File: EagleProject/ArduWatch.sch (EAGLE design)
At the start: 31 parts, among them IC1 DS1307Z, IC2 MCP73831, J1 FTS-105-01-L-D, Q1 32.768Hz, U2 ATMEGA328P-AU

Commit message: Starting Schematic
Starting Schematic in Eagle
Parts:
- LED1: value (none) -> Red
- LED2: value (none) -> Green
- renumbered PAD1 to USB+, PAD2 to USB-, PAD3 to BATTERY+, PAD4 to BATTERY-
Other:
- note added: "Battery 3,7V 140mAh"
- note added: "USB battery charger"
- note removed: "Bateria 3,7V"
- note removed: "Ładowarka USB"
- moved on the sheet: H1, H2, H3, H4, H5, J1, R7, U2

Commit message: Schematic V0.2.0
Schematic version 0.2.0
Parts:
- removed BATTERY+, BATTERY-: WIREPAD2,54/0,8, wirepad:WIREPAD2,54/0,8
- removed C4: 100nF, Kemet_By_element14_Batch_1:C1206C104K1RACTU
- removed H1, H2, H3, H4: MOUNT-HOLE3.0, holes:MOUNT-HOLE3.0
- removed LED2: Green, adafruit:LEDCHIPLED_1206
- removed R5: 10K Ohms, Multicomp_By_element14_Batch_1:MC0.125W12061%10K
- removed R6: 4.7 KOhm, Panasonic_By_element14_Batch_1:ERJ-8ENF4701V
- removed U$1: BATERY3,7V, Podreczne:BATERY3,7V
- removed U2: ATMEGA328P-AU, Atmel_By_element14_Batch_1-00:ATMEGA328P-AU
- added B+, B-: WIREPAD2,54/0,8, wirepad:WIREPAD2,54/0,8
- added C5: 0.1µF, AVX_By_element14_Batch_1:1206YC104KAT2A
- added U1: ATMEGA328P_TQFP, SparkFun-DigitalIC:ATMEGA328P_TQFP
- S1: value (none) -> Button1
- S2: value (none) -> Button2
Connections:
- removed net N$7: LED2.A, R6.R2
- removed net SQW: IC1.SQW, LED2.C, R5.R2
- new net D10: 1,3"OLED1.CS, U1.PB2(SS/OC1B)
- new net D8: 1,3"OLED1.RST, U1.PB0(ICP)
- new net D9: 1,3"OLED1.DC, U1.PB1(OC1A)
- net BUTTON1: now also U1.PD2(INT0)
- net BUTTON2: now also U1.PD3(INT1)
- net D11: now also 1,3"OLED1.D1, U1.PB3(MOSI/OC2)
- net D12: now also U1.PB4(MISO)
- net D13: now also 1,3"OLED1.D0, U1.PB5(SCK)
- net GND: now also 1,3"OLED1.GND, B-.P, C5.C1, U1.AGND, U1.GND@3, U1.GND@5; no longer BATTERY-.P, C4.C1, R6.R1, U$1.-
- net N$2: now also Q1.2; no longer Q1.1
- net N$5: now also Q1.1; no longer Q1.2
- net RESET: now also U1.PC6(/RESET); no longer U2.PC6
- net SCL: now also U1.PC5(ADC5/SCL)
- net SDA: now also U1.PC4(ADC4/SDA)
- net VCC: now also 1,3"OLED1.VCC, B+.P, C5.C2, U1.AVCC, U1.PC0(ADC0), U1.VCC@4, U1.VCC@6; no longer BATTERY+.P, C4.C2, R5.R1, U$1.+
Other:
- note added: "Buttons"
- note added: "Power"
- note removed: "Battery 3,7V 140mAh"
- note removed: "Przyciski"
- note removed: "Ładowanie baterii"
- moved on the sheet: C1, C2, C3, H5, IC2, LED1, Q1, R1, R2, R7, USB+, USB-

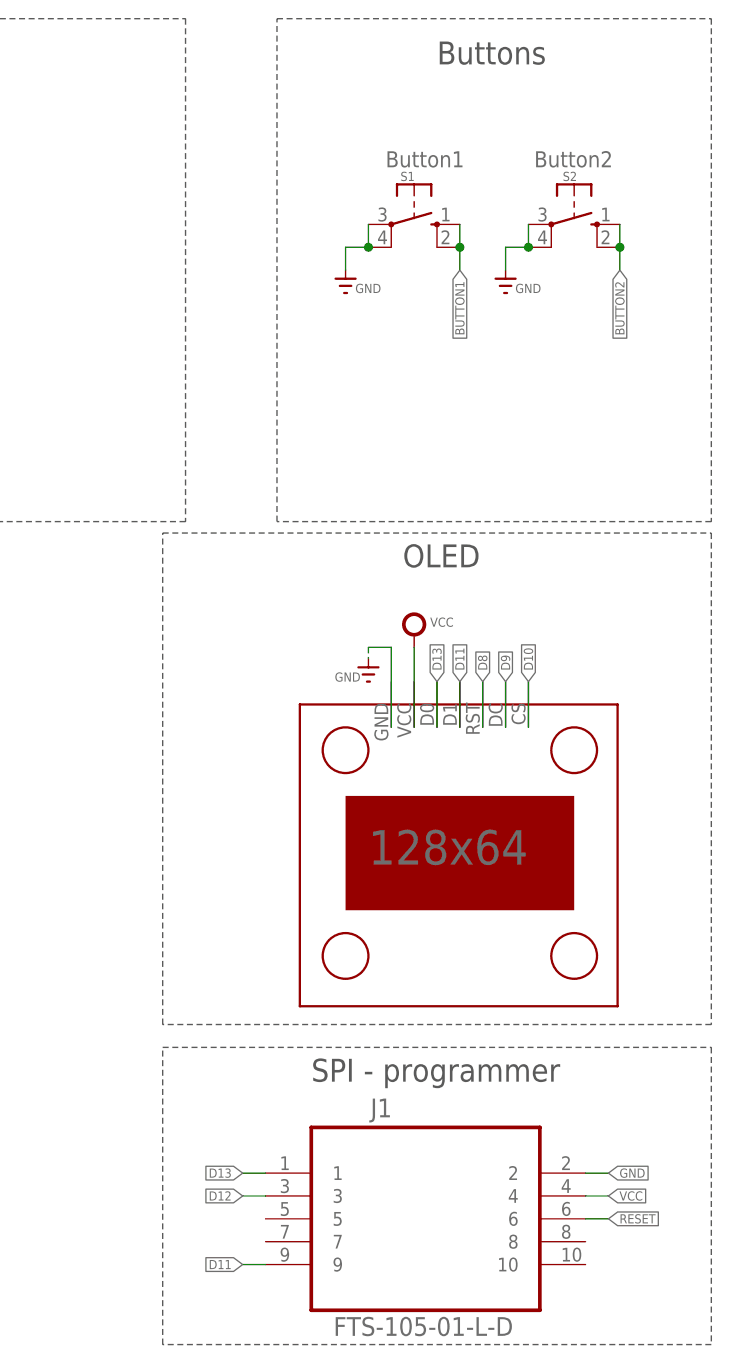
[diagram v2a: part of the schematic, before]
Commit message: Board V0.1.0
Update board to version 0.1.0
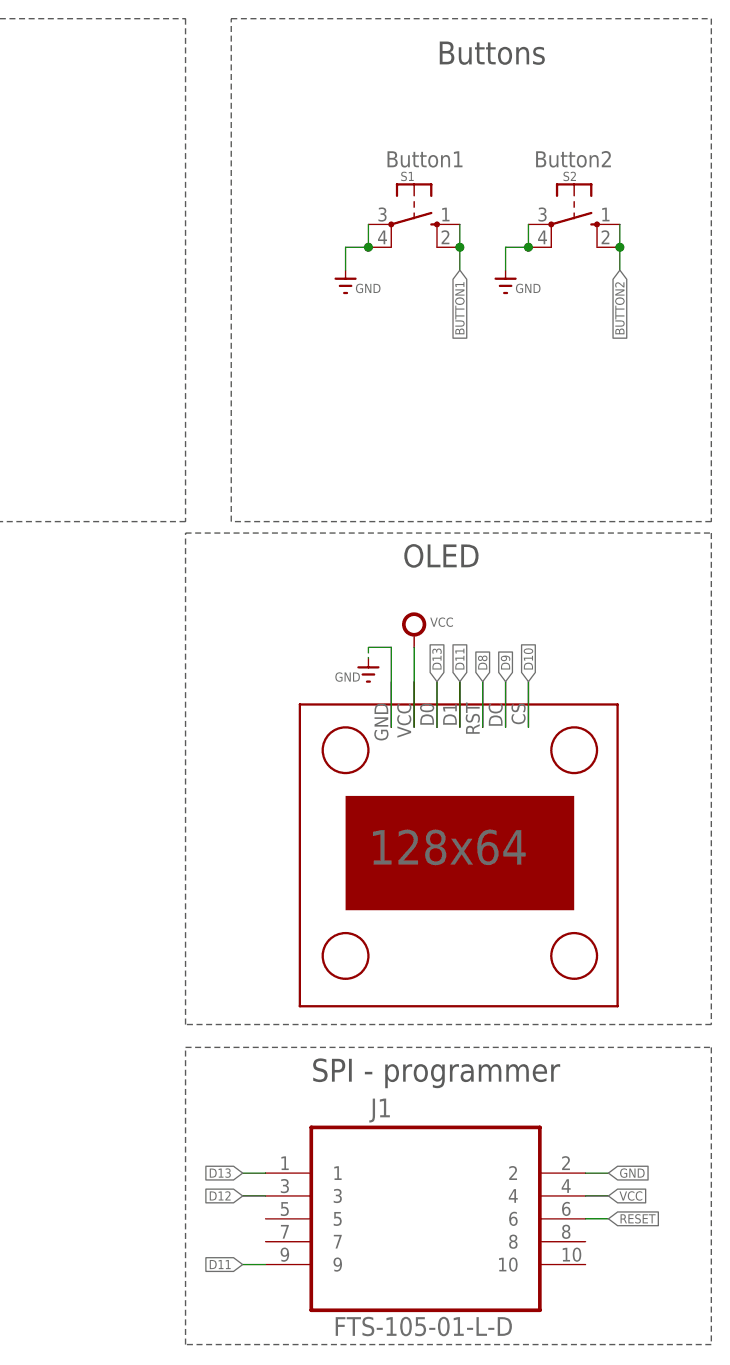
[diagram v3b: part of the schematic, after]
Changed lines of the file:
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@@
 <wire x1="101.6" y1="119.38" x2="101.6" y2="175.26" width="0.1524" layer="97" style="longdash"/>
 <text x="142.24" y="170.18" size="2.54" layer="97">RTC</text>
-<wire x1="200.66" y1="175.26" x2="248.92" y2="175.26" width="0.1524" layer="97" style="longdash"/>
+<wire x1="195.58" y1="175.26" x2="248.92" y2="175.26" width="0.1524" layer="97" style="longdash"/>
 <wire x1="248.92" y1="175.26" x2="248.92" y2="119.38" width="0.1524" layer="97" style="longdash"/>
-<wire x1="248.92" y1="119.38" x2="200.66" y2="119.38" width="0.1524" layer="97" style="longdash"/>
-<wire x1="200.66" y1="119.38" x2="200.66" y2="175.26" width="0.1524" layer="97" style="longdash"/>
+<wire x1="248.92" y1="119.38" x2="195.58" y2="119.38" width="0.1524" layer="97" style="longdash"/>
+<wire x1="195.58" y1="119.38" x2="195.58" y2="175.26" width="0.1524" layer="97" style="longdash"/>
 <text x="218.44" y="170.18" size="2.54" layer="97">Buttons</text>
-<wire x1="187.96" y1="118.11" x2="248.92" y2="118.11" width="0.1524" layer="97" style="longdash"/>
+<wire x1="190.5" y1="118.11" x2="248.92" y2="118.11" width="0.1524" layer="97" style="longdash"/>
 <wire x1="248.92" y1="118.11" x2="248.92" y2="63.5" width="0.1524" layer="97" style="longdash"/>
-<wire x1="248.92" y1="63.5" x2="187.96" y2="63.5" width="0.1524" layer="97" style="longdash"/>
-<wire x1="187.96" y1="63.5" x2="187.96" y2="118.11" width="0.1524" layer="97" style="longdash"/>
+<wire x1="248.92" y1="63.5" x2="190.5" y2="63.5" width="0.1524" layer="97" style="longdash"/>
+<wire x1="190.5" y1="63.5" x2="190.5" y2="118.11" width="0.1524" layer="97" style="longdash"/>
 <text x="214.63" y="114.3" size="2.54" layer="97">OLED</text>
-<wire x1="187.96" y1="60.96" x2="248.92" y2="60.96" width="0.1524" layer="97" style="longdash"/>
+<wire x1="190.5" y1="60.96" x2="248.92" y2="60.96" width="0.1524" layer="97" style="longdash"/>
 <wire x1="248.92" y1="60.96" x2="248.92" y2="27.94" width="0.1524" layer="97" style="longdash"/>
-<wire x1="248.92" y1="27.94" x2="187.96" y2="27.94" width="0.1524" layer="97" style="longdash"/>
-<wire x1="187.96" y1="27.94" x2="187.96" y2="60.96" width="0.1524" layer="97" style="longdash"/>
+<wire x1="248.92" y1="27.94" x2="190.5" y2="27.94" width="0.1524" layer="97" style="longdash"/>
+<wire x1="190.5" y1="27.94" x2="190.5" y2="60.96" width="0.1524" layer="97" style="longdash"/>
 <text x="204.47" y="57.15" size="2.54" layer="97">SPI - programmer</text>
 </plain>

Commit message: PCB release
PCB release
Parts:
- H5: value MOUNT-HOLE4.1 -> MOUNT-HOLE3.0; device holes:MOUNT-HOLE4.1 -> holes:MOUNT-HOLE3.0
- USB+, USB-: value WIREPAD2,54/0,8 -> WIREPAD3,81/1,1; device wirepad:WIREPAD2,54/0,8 -> wirepad:WIREPAD3,81/1,1
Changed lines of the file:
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@@
 <part name="Q1" library="crystal" deviceset="CRYSTAL" device="TC26H" value="32.768Hz"/>
 <part name="IC2" library="microchip-update" deviceset="MCP73831" device=""/>
-<part name="USB+" library="wirepad" deviceset="WIREPAD" device="2,54/0,8"/>
-<part name="USB-" library="wirepad" deviceset="WIREPAD" device="2,54/0,8"/>
+<part name="USB+" library="wirepad" deviceset="WIREPAD" device="3,81/1,1" value="WIREPAD3,81/1,1"/>
+<part name="USB-" library="wirepad" deviceset="WIREPAD" device="3,81/1,1" value="WIREPAD3,81/1,1"/>
 <part name="GND1" library="supply" deviceset="GND" device=""/>
 <part name="V1" library="supply" deviceset="VUSB" device=""/>
@@
 <part name="V7" library="supply" deviceset="VCC" device=""/>
 <part name="R7" library="Multicomp_By_element14_Batch_1" deviceset="MC0.125W12061%10K" device="" value="10K Ohms"/>
-<part name="H5" library="holes" deviceset="MOUNT-HOLE" device="4.1"/>
+<part name="H5" library="holes" deviceset="MOUNT-HOLE" device="3.0" value="MOUNT-HOLE3.0"/>
 <part name="J1" library="SAMTEC-HTSW-FTxx_By_element14_Batch_1" deviceset="FTS-105-01-L-D" device=""/>
 <part name="FRAME1" library="frames" deviceset="A4L-LOC" device="" value="Frame"/>
@@
 <sheet>
 <plain>
-<text x="17.78" y="160.02" size="1.778" layer="97">USB battery charger</text>
+<text x="12.7" y="154.94" size="1.778" layer="97">USB battery charger</text>
 <wire x1="5.08" y1="175.26" x2="99.06" y2="175.26" width="0.1524" layer="97" style="longdash"/>
 <wire x1="99.06" y1="175.26" x2="99.06" y2="119.38" width="0.1524" layer="97" style="longdash"/>

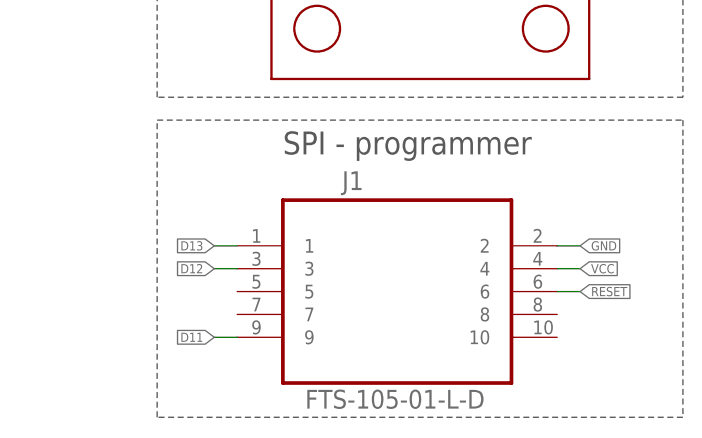
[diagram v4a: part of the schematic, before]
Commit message: PCB - SPI as Arduino
Change connector for SPI Target
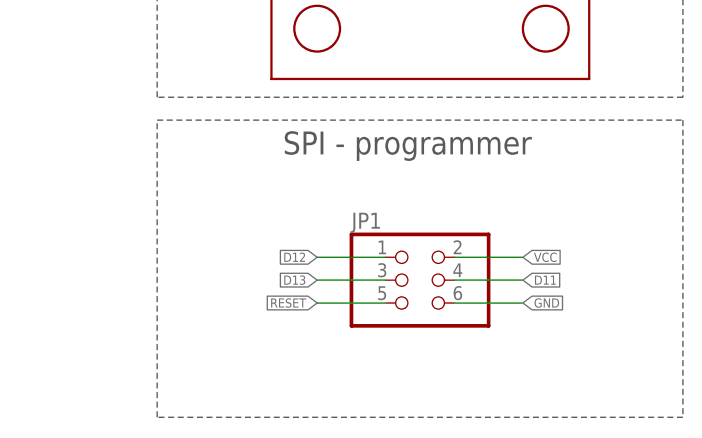
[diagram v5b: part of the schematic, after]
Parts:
- removed J1: FTS-105-01-L-D, SAMTEC-HTSW-FTxx_By_element14_Batch_1:FTS-105-01-L-D
- added JP1: (no value), pinhead:PINHD-2X3
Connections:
- net D11: now also JP1.4; no longer J1.9
- net D12: now also JP1.1; no longer J1.3
- net D13: now also JP1.3; no longer J1.1
- net GND: now also JP1.6; no longer J1.2
- net RESET: now also JP1.5; no longer J1.6
- net VCC: now also JP1.2; no longer J1.4
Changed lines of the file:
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@@
 <part name="R7" library="Multicomp_By_element14_Batch_1" deviceset="MC0.125W12061%10K" device="" value="10K Ohms"/>
 <part name="H5" library="holes" deviceset="MOUNT-HOLE" device="3.0" value="MOUNT-HOLE3.0"/>
-<part name="J1" library="SAMTEC-HTSW-FTxx_By_element14_Batch_1" deviceset="FTS-105-01-L-D" device=""/>
 <part name="FRAME1" library="frames" deviceset="A4L-LOC" device="" value="Frame"/>
 <part name="V6" library="supply" deviceset="VCC" device=""/>
@@
 <part name="GND11" library="supply" deviceset="GND" device=""/>
 <part name="V8" library="supply" deviceset="VCC" device=""/>
+<part name="JP1" library="pinhead" deviceset="PINHD-2X3" device=""/>
 </parts>
 <sheets>
@@
 <attribute name="VALUE" x="61.468" y="129.4638" size="1.016" layer="96" rot="R180"/>
 </instance>
-<instance part="J1" gate="A" x="217.17" y="44.45" smashed="yes">
-<attribute name="NAME" x="211.0486" y="53.1876" size="2.0828" layer="95" ratio="10" rot="SR0"/>
-<attribute name="VALUE" x="206.9338" y="28.9052" size="2.0828" layer="96" ratio="10" rot="SR0"/>
-</instance>
 <instance part="FRAME1" gate="G$1" x="0" y="0"/>
 <instance part="V6" gate="VCC" x="57.15" y="92.71" smashed="yes">
@@
 <attribute name="VALUE" x="126.238" y="92.456" size="1.016" layer="96"/>
 </instance>
+<instance part="JP1" gate="A" x="218.44" y="43.18"/>
 </instances>
 <busses>
@@
 </segment>
 <segment>
-<pinref part="J1" gate="A" pin="2"/>
-<wire x1="234.95" y1="46.99" x2="237.49" y2="46.99" width="0.1524" layer="91"/>
-<label x="237.49" y="46.99" size="1.016" layer="95" xref="yes"/>
-</segment>
-<segment>
 <pinref part="GND10" gate="1" pin="GND"/>
 <pinref part="C5" gate="A" pin="C1"/>
@@
 <junction x="68.58" y="39.37"/>
 </segment>
+<segment>
+<pinref part="JP1" gate="A" pin="6"/>
+<wire x1="223.52" y1="40.64" x2="231.14" y2="40.64" width="0.1524" layer="91"/>
+<label x="231.14" y="40.64" size="1.016" layer="95" xref="yes"/>
+</segment>
 </net>
 <net name="N$4" class="0">
@@
 <wire x1="71.12" y1="107.95" x2="71.12" y2="106.68" width="0.1524" layer="91"/>
 <pinref part="R7" gate="A" pin="R1"/>
-</segment>
-<segment>
-<pinref part="J1" gate="A" pin="4"/>
-<wire x1="234.95" y1="44.45" x2="237.49" y2="44.45" width="0.1524" layer="91"/>
-<label x="237.49" y="44.45" size="1.016" layer="95" xref="yes"/>
 </segment>
 <segment>
@@
 <pinref part="V8" gate="VCC" pin="VCC"/>
 </segment>
+<segment>
+<pinref part="JP1" gate="A" pin="2"/>
+<wire x1="223.52" y1="45.72" x2="231.14" y2="45.72" width="0.1524" layer="91"/>
+<label x="231.14" y="45.72" size="1.016" layer="95" xref="yes"/>
+</segment>
 </net>
 <net name="SCL" class="0">
@@
 </segment>
 <segment>
-<pinref part="J1" gate="A" pin="1"/>
-<wire x1="199.39" y1="46.99" x2="196.85" y2="46.99" width="0.1524" layer="91"/>
-<label x="196.85" y="46.99" size="1.016" layer="95" rot="R180" xref="yes"/>
-</segment>
-<segment>
 <pinref part="U1" gate="U$1" pin="PB5(SCK)"/>
 <wire x1="121.92" y1="34.29" x2="125.73" y2="34.29" width="0.1524" layer="91"/>
 <label x="125.73" y="34.29" size="1.016" layer="95" xref="yes"/>
 </segment>
+<segment>
+<pinref part="JP1" gate="A" pin="3"/>
+<wire x1="215.9" y1="43.18" x2="208.28" y2="43.18" width="0.1524" layer="91"/>
+<label x="208.28" y="43.18" size="1.016" layer="95" rot="R180" xref="yes"/>
+</segment>
 </net>
 <net name="D11" class="0">
@@
 </segment>
 <segment>
-<pinref part="J1" gate="A" pin="9"/>
-<wire x1="199.39" y1="36.83" x2="196.85" y2="36.83" width="0.1524" layer="91"/>
-<label x="196.85" y="36.83" size="1.016" layer="95" rot="R180" xref="yes"/>
-</segment>
-<segment>
 <pinref part="U1" gate="U$1" pin="PB3(MOSI/OC2)"/>
 <wire x1="121.92" y1="39.37" x2="125.73" y2="39.37" width="0.1524" layer="91"/>
 <label x="125.73" y="39.37" size="1.016" layer="95" xref="yes"/>
+</segment>
+<segment>
+<pinref part="JP1" gate="A" pin="4"/>
+<wire x1="223.52" y1="43.18" x2="231.14" y2="43.18" width="0.1524" layer="91"/>
+<label x="231.14" y="43.18" size="1.016" layer="95" xref="yes"/>
 </segment>
 </net>
@@
 </segment>
 <segment>
-<pinref part="J1" gate="A" pin="6"/>
-<wire x1="234.95" y1="41.91" x2="237.49" y2="41.91" width="0.1524" layer="91"/>
-<label x="237.49" y="41.91" size="1.016" layer="95" xref="yes"/>
+<pinref part="JP1" gate="A" pin="5"/>
+<wire x1="215.9" y1="40.64" x2="208.28" y2="40.64" width="0.1524" layer="91"/>
+<label x="208.28" y="40.64" size="1.016" layer="95" rot="R180" xref="yes"/>
 </segment>
 </net>
 <net name="D12" class="0">
-<segment>
-<pinref part="J1" gate="A" pin="3"/>
-<wire x1="199.39" y1="44.45" x2="196.85" y2="44.45" width="0.1524" layer="91"/>
-<label x="196.85" y="44.45" size="1.016" layer="95" rot="R180" xref="yes"/>
-</segment>
 <segment>
 <pinref part="U1" gate="U$1" pin="PB4(MISO)"/>
@@
 <label x="125.73" y="36.83" size="1.016" layer="95" xref="yes"/>
 </segment>
-</net>
+<segment>
+<pinref part="JP1" gate="A" pin="1"/>
+<wire x1="215.9" y1="45.72" x2="208.28" y2="45.72" width="0.1524" layer="91"/>
+<label x="208.28" y="45.72" size="1.016" layer="95" rot="R180" xref="yes"/>
+</segment>
+</net>
